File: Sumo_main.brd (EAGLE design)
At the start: 30 x 50 mm, 41 parts, among them U1 ATMEGA8U2AU, U2 SN65HVD3082, U3 LM339D, X2 RS485, X4 IR Sensor 1, X5 IR Sensor 2, X6 IR Sensor 3, Y1 16MHz

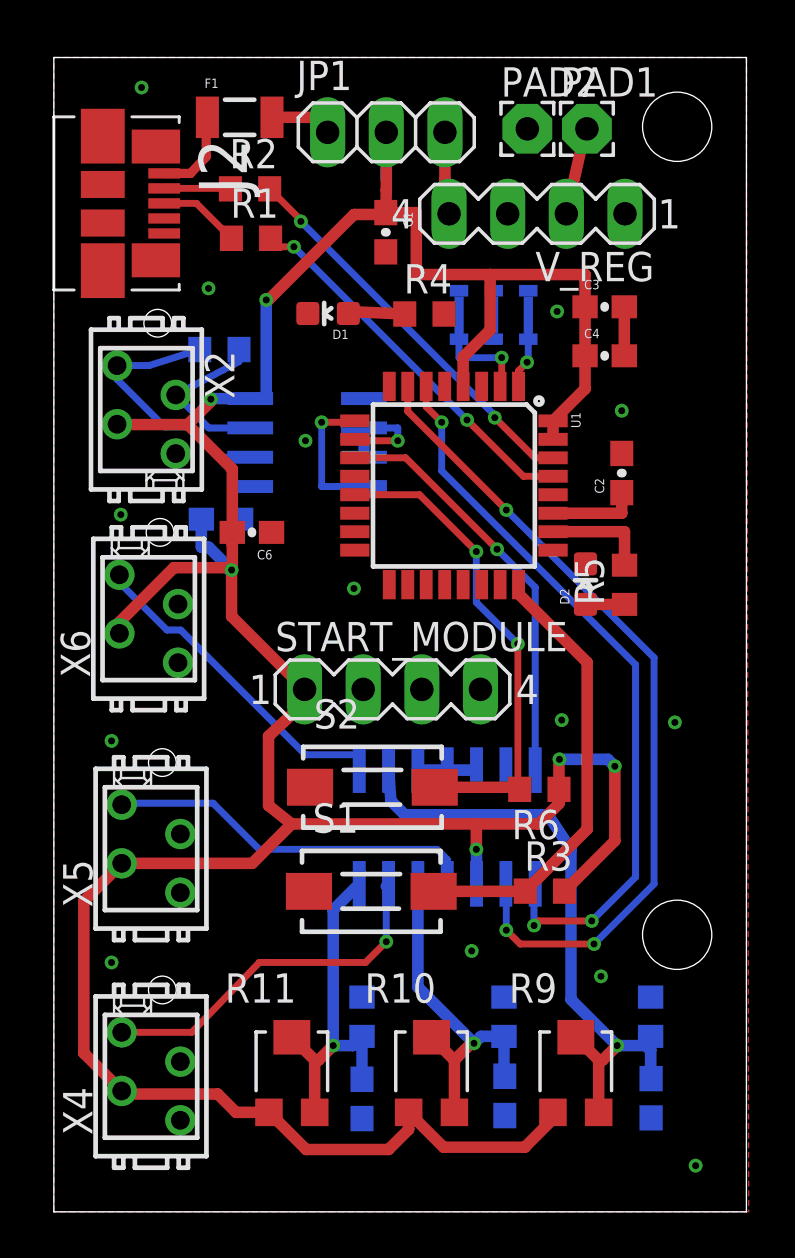
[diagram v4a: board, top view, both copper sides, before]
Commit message: Made the board more compact.
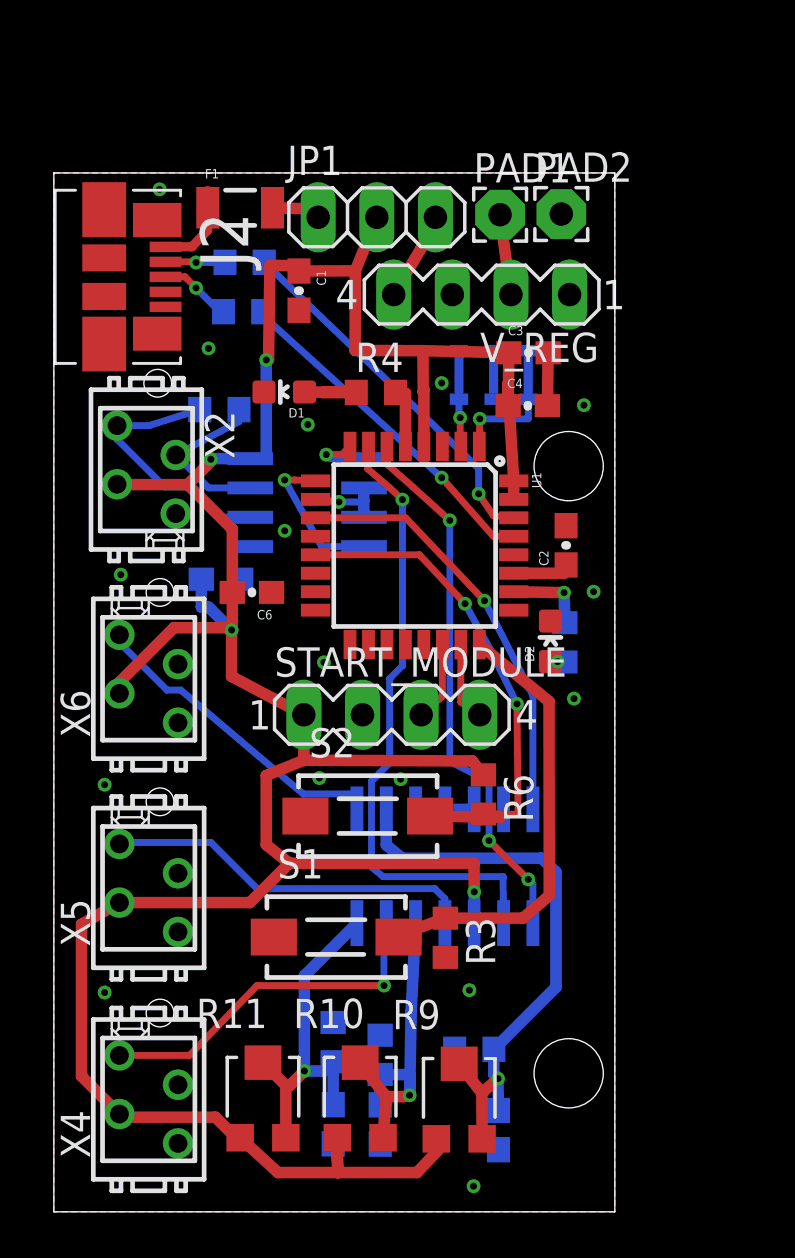
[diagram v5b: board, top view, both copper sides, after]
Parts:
- moved R12 7.77 mm to (18.2, 7.04), turned to 180 degrees
- moved C8 6.75 mm to (19.3, 3.54)
- moved R13 5.62 mm to (14.1, 6.80)
- moved C9 5.53 mm to (14.1, 3.78)
- moved PAD1 5.29 mm to (19.3, 43.2)
- moved R9 5.18 mm to (17.6, 4.76)
- moved R3 4.76 mm to (17.0, 11.9), turned to 270 degrees
- moved C1 4.53 mm to (10.6, 39.9)
- moved V_REG 4.24 mm to (18.5, 39.7)
- moved R4 4.00 mm to (13.9, 35.5)
- moved PAD2 3.97 mm to (22.0, 43.2)
- moved C4 3.97 mm to (20.5, 34.9)
- moved C2 3.95 mm to (22.2, 28.9)
- moved F1 3.92 mm to (8.07, 43.5)
- moved D1 3.89 mm to (9.98, 35.5)
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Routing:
- net VCC: track 144.8 -> 131.0 mm, vias 6 -> 4
- net COMP_OUT1: track 32.1 -> 23.7 mm
- net COMP_OUT2: track 35.7 -> 27.3 mm, vias 3 -> 1
- net KILL: track 0.00 -> 3.47 mm
- net START: track 0.00 -> 3.46 mm
- net RX: track 0.00 -> 2.88 mm, vias 0 -> 1
- net LED1: track 0.00 -> 2.74 mm
- net N$5: track 3.34 -> 5.80 mm
- net VREF3: track 27.6 -> 25.4 mm
- net N$10: track 2.49 -> 4.62 mm
- net N$6: track 5.02 -> 3.16 mm
- net DE: track 5.21 -> 3.41 mm
- net D+: track 16.5 -> 14.9 mm, vias 2 -> 1
- net N$7: track 3.87 -> 2.55 mm
- net N$13: track 21.1 -> 22.4 mm
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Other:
- board size 30 x 50 mm -> 24.3 x 45 mm

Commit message: Added additional button for starting. Changed IR sensors' micromatches to pinheaders.
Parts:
- removed X4: IR Sensor 1, con-amp-micromatch:MICROMATCH-4
- removed X5: IR Sensor 2, con-amp-micromatch:MICROMATCH-4
- removed X6: IR Sensor 3, con-amp-micromatch:MICROMATCH-4
- added IR1, IR2, IR3: (no value), con-lstb:MA03-1
- added R7: 10K, resistor:R0603
- added START_BTN: DTSM-3, switch-tact:DTSM-3
- renumbered R3 to RESET_BTN, R6 to BTL_BTN
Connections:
- new net N$8: R7.1, START_BTN.2, U1.14
- net GND: now also IR1.2, IR3.2, START_BTN.1; no longer X4.2, X5.2, X6.2
- net V01: now also IR1.3; no longer X4.1
- net V02: now also IR2.3; no longer X5.1
- net V03: now also IR3.3; no longer X6.1
- net VCC: now also IR1.1, IR2.1, IR3.1, R7.2; no longer X4.3, X5.3, X6.3
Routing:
- net N$8: track 0.00 -> 26.7 mm, vias 0 -> 3
- net V01: track 15.9 -> 10.8 mm
- net VCC: track 131.0 -> 130.3 mm, vias 4 -> 5
- net GND: vias 16 -> 13

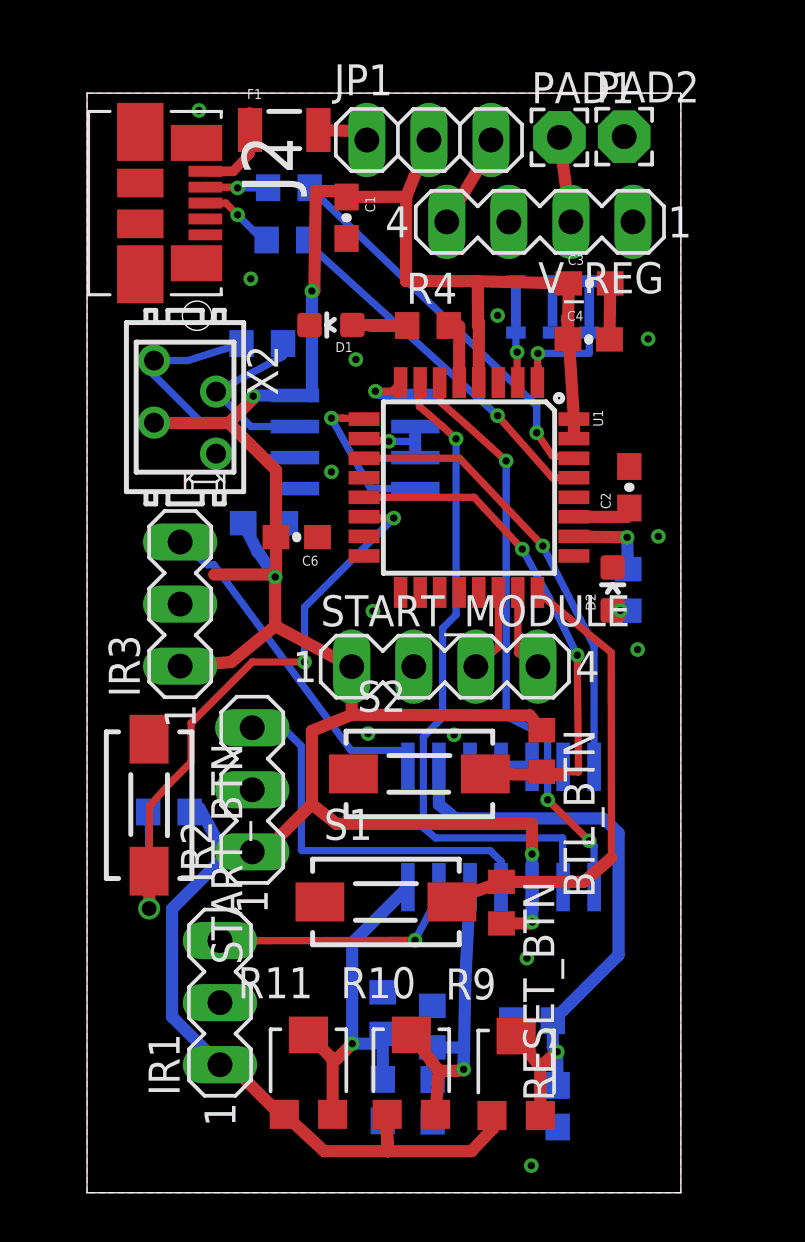
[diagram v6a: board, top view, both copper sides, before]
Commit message: Add two IR reflection sensors to detect lines.
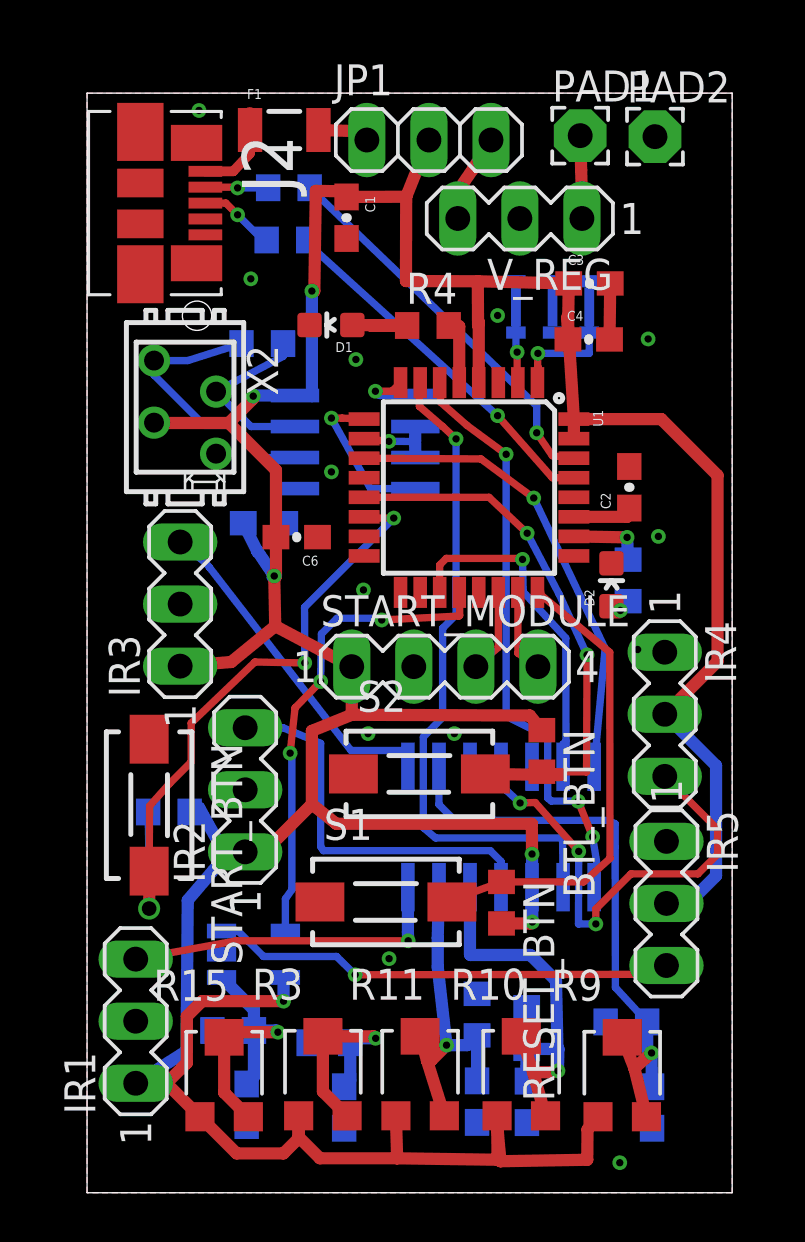
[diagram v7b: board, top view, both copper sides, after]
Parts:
- added C10, C11: 1uF, SparkFun-Capacitors:0603-CAP
- added IC1: TL331, linear:DBV-R-PDSO-G5
- added IR4, IR5: (no value), con-lstb:MA03-1
- added R15, R3: 10KOHM, Panasonic-Trimmer_Potentiometers:POT_EVM3W
- added R16, R6: 500R, resistor:R0603
- V_REG: device con-lstb:MA04-1 -> con-lstb:MA03-1
- moved R11 4.57 mm to (13.6, 4.75)
- moved R10 4.50 mm to (17.8, 4.75)
- moved R9 4.34 mm to (21.9, 4.71)
- moved C7 3.86 mm to (16.0, 3.73)
- moved R14 3.86 mm to (16.0, 7.29)
- moved C9 3.86 mm to (18.0, 3.72)
- moved R13 3.86 mm to (18.0, 6.74)
- moved C8 3.86 mm to (23.1, 3.49)
- moved R12 3.86 mm to (22.1, 6.99)
- moved IR1 3.53 mm to (1.99, 7.02)
- moved PAD2 1.26 mm to (23.2, 43.2)
- moved PAD1 0.85 mm to (20.2, 43.3)
- moved V_REG 0.83 mm to (17.7, 39.9)
- moved R5 0.39 mm to (22.1, 25.1)
- moved IR2 0.29 mm to (6.47, 16.5)
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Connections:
- new net COMP_OUT4: U1.19, U3.13
- new net COMP_OUT5: IC1.4, U1.20
- new net V04: IR4.3, U3.11
- new net V05: IC1.3, IR5.3
- new net VREF4: C10.1, R3.2, R3.3, R6.2, U3.10
- new net VREF5: C11.1, IC1.1, R15.2, R15.3, R16.2
- net GND: now also C10.2, C11.2, IC1.2, IR4.1, IR5.1, R16.1, R6.1, V_REG.2; no longer U3.10, U3.11, V_REG.3
- net N$14: now also V_REG.3; no longer V_REG.4
- net N$23: now also V_REG.1; no longer V_REG.2
- net V01: now also U3.7; no longer U3.6
- net VCC: now also IC1.5, IR4.2, IR5.2, R15.1, R3.1
- net VREF1: now also U3.6; no longer U3.7
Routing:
- net VCC: track 130.3 -> 177.3 mm, vias 5 -> 6
- net COMP_OUT5: track 0.00 -> 19.6 mm, vias 0 -> 3
- net V04: track 0.00 -> 19.4 mm, vias 0 -> 3
- net V05: track 0.00 -> 19.1 mm, vias 0 -> 1
- net COMP_OUT4: track 0.00 -> 13.9 mm, vias 0 -> 1
- net VREF5: track 0.00 -> 12.0 mm, vias 0 -> 1
- net VREF4: track 0.00 -> 8.87 mm, vias 0 -> 1
- net VREF2: track 15.6 -> 18.3 mm
- net V01: track 10.8 -> 13.4 mm
- net GND: track 4.83 -> 2.29 mm
- net VREF1: track 15.3 -> 14.2 mm
- net N$13: track 22.4 -> 23.2 mm
- net COMP_OUT3: track 18.4 -> 19.1 mm
- net VREF3: track 25.4 -> 24.8 mm
- net COMP_OUT1: track 23.7 -> 24.3 mm
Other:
- board size 24.3 x 45 mm -> 26.4 x 45 mm

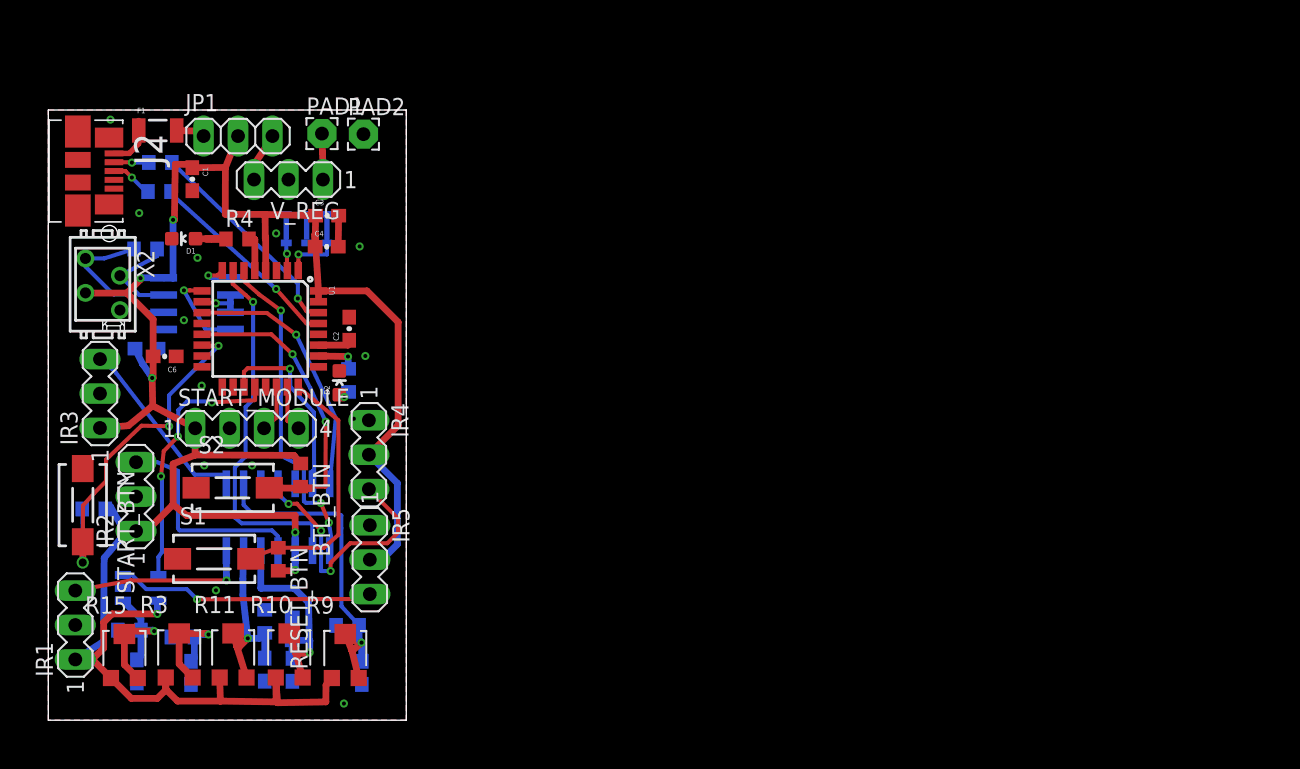
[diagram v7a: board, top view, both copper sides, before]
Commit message: Start arranging new board.
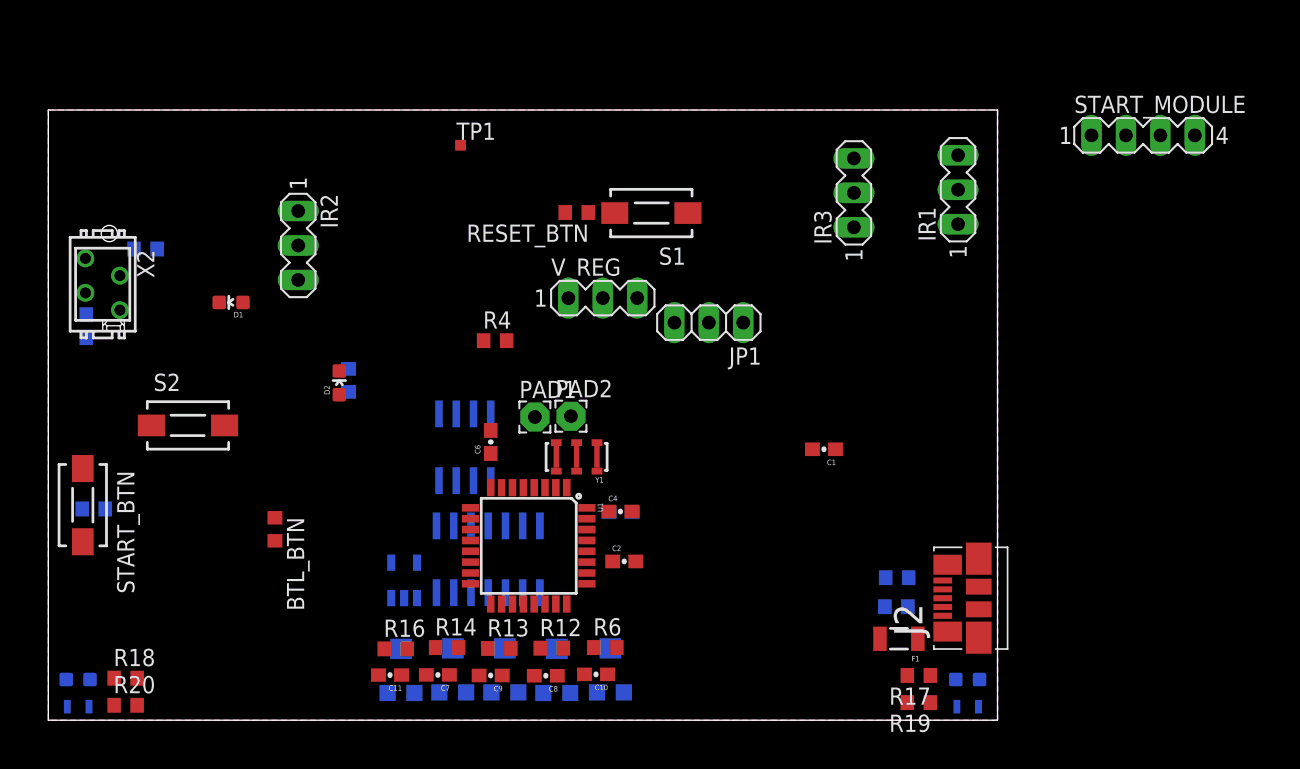
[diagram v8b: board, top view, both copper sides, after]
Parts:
- removed IR4, IR5: (no value), con-lstb:MA03-1
- added D3, D4: (no value), SparkFun-LED:LED-0603
- added R17, R18: 1K, resistor:R0603
- added R19, R20: 47K, resistor:R0603
- added T1, T2: 0603-PHOTO-TRANS, Phototransistor 0603:PHOTOTRANSISTOR
- added TP1: TPSQTP08SQ, testpad:TP08SQ
- moved IR1 72.6 mm to (67.1, 39.1)
- moved START_MODULE 69.5 mm to (80.7, 43.1)
- moved J2 68.8 mm to (66.0, 9.00), turned to 90 degrees
- moved F1 66.3 mm to (62.7, 6.01), turned to 180 degrees
- moved R2 63.4 mm to (62.5, 8.37), turned to 0 degrees
- moved R1 61.4 mm to (62.6, 10.5), turned to 0 degrees
- moved IR3 57.5 mm to (59.4, 38.9)
- moved C1 50.7 mm to (57.2, 20.0), turned to 180 degrees
- moved S1 41.1 mm to (44.5, 37.4), turned to 180 degrees
- moved JP1 37.3 mm to (48.7, 29.3), turned to 180 degrees
- moved RESET_BTN 33.7 mm to (39.0, 37.4), turned to 180 degrees
- moved R3 31.8 mm to (41.5, 3.65), flipped to the bottom
- moved R6 31.2 mm to (41.1, 5.36), flipped to the top, turned to 0 degrees
- moved C3 30.8 mm to (42.2, 15.3), flipped to the bottom, turned to 180 degrees
- moved C10 29.9 mm to (40.4, 3.38), flipped to the top, turned to 180 degrees
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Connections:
- net VREF4 renamed LN1REF
- net VREF5 renamed LN2REF
- removed net V04: IR4.3, U3.11
- removed net V05: IC1.3, IR5.3
- new net LN1: R19.1, T1.COLLECTOR, U3.11
- new net LN2: IC1.3, R20.1, T2.COLLECTOR
- new net N$15: D3.A, R17.1
- new net N$17: U1.25
- new net N$18: D4.A, R18.1
- net COMP_OUT1: now also U1.21; no longer U1.6
- net COMP_OUT2: now also U1.20; no longer U1.7
- net COMP_OUT3: now also U1.19; no longer U1.11
- net COMP_OUT4: now also U1.18; no longer U1.19
- net COMP_OUT5: now also U1.11; no longer U1.20
- net GND: now also D3.C, D4.C, IR2.2, T1.EMITTER, T2.EMITTER; no longer IR4.1, IR5.1
- net VCC: now also R17.2, R18.2, R19.2, R20.2; no longer IR4.2, IR5.2
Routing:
- net VCC: track 177.3 -> 0.00 mm, vias 6 -> 0
- net COMP_OUT2: track 27.3 -> 0.00 mm, vias 1 -> 0
- net N$8: track 26.7 -> 0.00 mm, vias 3 -> 0
- net VREF3: track 24.8 -> 0.00 mm, vias 1 -> 0
- net COMP_OUT1: track 24.3 -> 0.00 mm, vias 3 -> 0
- net N$13: track 23.2 -> 0.00 mm, vias 2 -> 0
- net COMP_OUT5: track 19.6 -> 0.00 mm, vias 3 -> 0
- net V04: track 19.4 -> 0.00 mm, vias 3 -> 0
- net N$4: track 19.4 -> 0.00 mm
- net COMP_OUT3: track 19.1 -> 0.00 mm, vias 1 -> 0
- net V05: track 19.1 -> 0.00 mm, vias 1 -> 0
- net VREF2: track 18.3 -> 0.00 mm, vias 1 -> 0
- net V02: track 16.1 -> 0.00 mm
- net D-: track 16.0 -> 0.00 mm, vias 1 -> 0
- net D+: track 14.9 -> 0.00 mm, vias 1 -> 0
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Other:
- board size 26.4 x 45 mm -> 70 x 45 mm
